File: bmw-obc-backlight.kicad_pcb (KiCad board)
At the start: 2 copper layers, 12 x 59 mm, 4 parts, among them J1 Conn_01x02

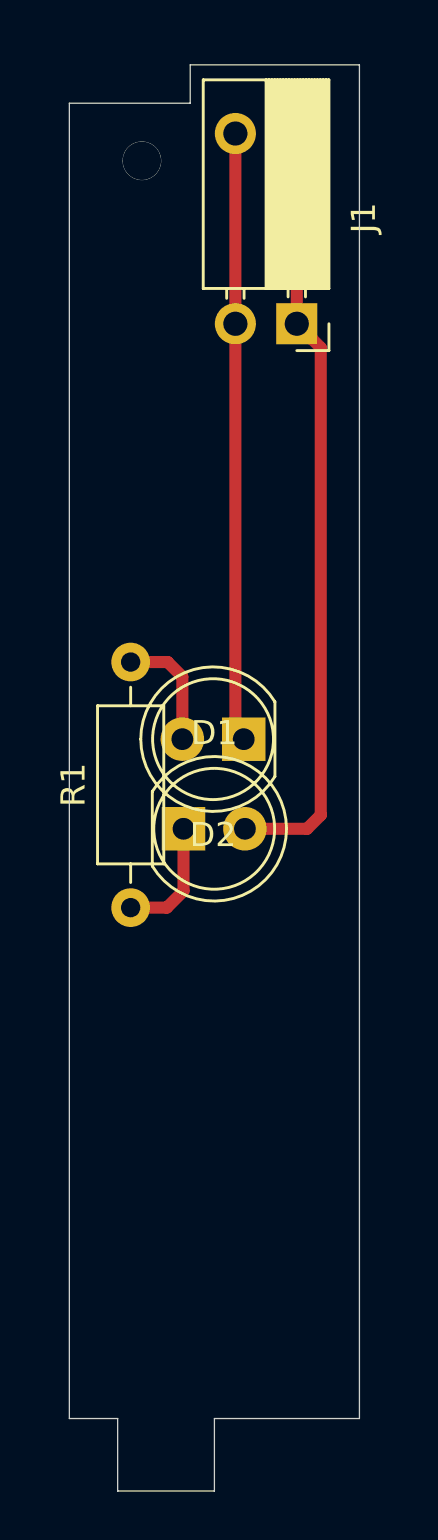
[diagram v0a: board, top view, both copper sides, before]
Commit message: Swapped resistor to SMT. There isn't enough space for a through hole unless it's between the LED legs.
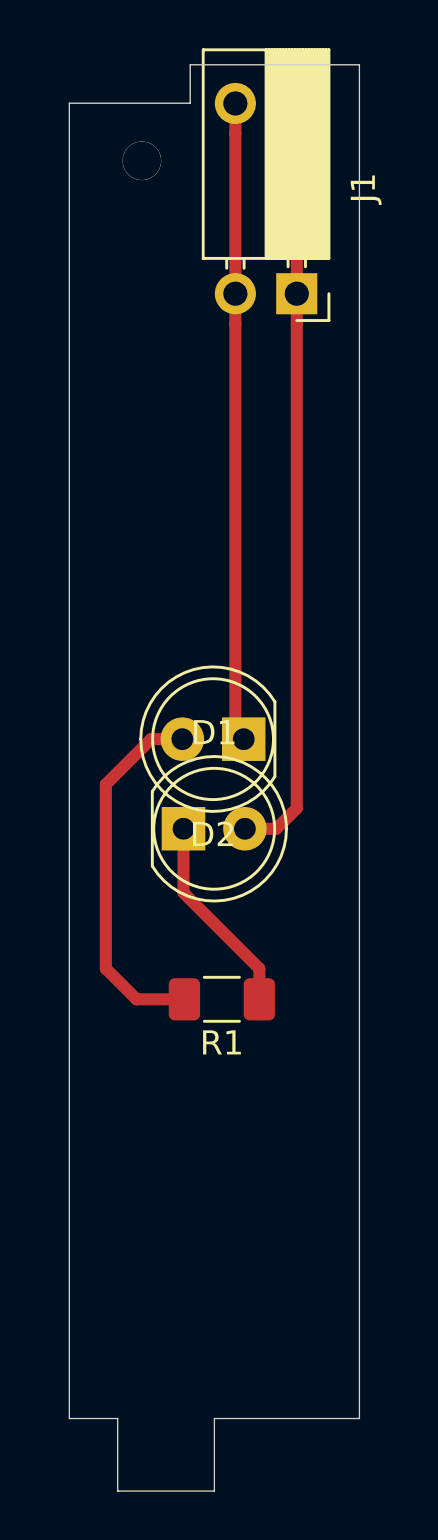
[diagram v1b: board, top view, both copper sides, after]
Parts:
- R1: footprint Resistor_THT:R_Axial_DIN0207_L6.3mm_D2.5mm_P10.16mm_Horizontal -> Resistor_SMD:R_1206_3216Metric_Pad1.30x1.75mm_HandSolder
- moved R1 5.35 mm to (21.3, 52.1), turned to 180 degrees
- moved J1 1.24 mm to (24.4, 22.9)
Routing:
- net Net-(D2-Pad2): track 4.97 -> 15.3 mm
- net Net-(D1-Pad1): track 5.04 -> 8.35 mm
- net Net-(D2-Pad1): track 25.2 -> 26.4 mm
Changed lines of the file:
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@@
     (thickness 1.6)
     (drawings 11)
-    (tracks 15)
+    (tracks 18)
     (zones 0)
     (modules 4)
@@
     (pad_to_mask_clearance 0)
     (aux_axis_origin 0 0)
-    (visible_elements FFFFFF7F)
+    (visible_elements 7FFFFFFF)
     (pcbplotparams
       (layerselection 0x010f0_ffffffff)
@@
     (add_net "Net-(D2-Pad2)")
   )
+  (module Resistor_SMD:R_1206_3216Metric_Pad1.30x1.75mm_HandSolder (layer F.Cu)
+    (at 21.31 52.07 180)
+    (descr "Resistor SMD 1206 (3216 Metric), square (rectangular) end terminal, IPC_7351 nominal with elongated pad for handsoldering. (Body size source: IPC-SM-782 page 72, https://www.pcb-3d.com/wordpress/wp-content/uploads/ipc-sm-782a_amendment_1_and_2.pdf), generated with kicad-footprint-generator")
+    (tags "resistor handsolder")
+    (attr smd)
+    (fp_text reference R1 (at 0 -1.82) (layer F.SilkS)
+      (effects (font (size 1 1) (thickness 0.15)))
+    )
+    (fp_text value 10000 (at 0 1.82) (layer F.Fab)
+      (effects (font (size 1 1) (thickness 0.15)))
+    )
+    (fp_text user %R (at 0 0) (layer F.Fab)
+      (effects (font (size 0.8 0.8) (thickness 0.12)))
+    )
+    (fp_line (start -1.6 0.8) (end -1.6 -0.8) (layer F.Fab) (width 0.1))
+    (fp_line (start -1.6 -0.8) (end 1.6 -0.8) (layer F.Fab) (width 0.1))
+    (fp_line (start 1.6 -0.8) (end 1.6 0.8) (layer F.Fab) (width 0.1))
+    (fp_line (start 1.6 0.8) (end -1.6 0.8) (layer F.Fab) (width 0.1))
+    (fp_line (start -0.727064 -0.91) (end 0.727064 -0.91) (layer F.SilkS) (width 0.12))
+    (fp_line (start -0.727064 0.91) (end 0.727064 0.91) (layer F.SilkS) (width 0.12))
+    (fp_line (start -2.45 1.12) (end -2.45 -1.12) (layer F.CrtYd) (width 0.05))
+    (fp_line (start -2.45 -1.12) (end 2.45 -1.12) (layer F.CrtYd) (width 0.05))
+    (fp_line (start 2.45 -1.12) (end 2.45 1.12) (layer F.CrtYd) (width 0.05))
+    (fp_line (start 2.45 1.12) (end -2.45 1.12) (layer F.CrtYd) (width 0.05))
+    (pad 2 smd roundrect (at 1.55 0 180) (size 1.3 1.75) (layers F.Cu F.Paste F.Mask) (roundrect_rratio 0.1923076923076923)
+      (net 3 "Net-(D2-Pad2)"))
+    (pad 1 smd roundrect (at -1.55 0 180) (size 1.3 1.75) (layers F.Cu F.Paste F.Mask) (roundrect_rratio 0.1923076923076923)
+      (net 1 "Net-(D1-Pad1)"))
+    (model ${KISYS3DMOD}/Resistor_SMD.3dshapes/R_1206_3216Metric.wrl
+      (at (xyz 0 0 0))
+      (scale (xyz 1 1 1))
+      (rotate (xyz 0 0 0))
+    )
+  )
   (module LED_THT:LED_D5.0mm (layer F.Cu)
     (at 19.722532 45.015429)
@@
       (effects (font (size 1 1) (thickness 0.15)))
     )
-    (fp_text user %R (at 1.25 0) (layer F.Fab)
-      (effects (font (size 0.8 0.8) (thickness 0.2)))
-    )
-    (fp_arc (start 1.27 0) (end -1.29 1.54483) (angle -148.9) (layer F.SilkS) (width 0.12))
-    (fp_arc (start 1.27 0) (end -1.29 -1.54483) (angle 148.9) (layer F.SilkS) (width 0.12))
-    (fp_arc (start 1.27 0) (end -1.23 -1.469694) (angle 299.1) (layer F.Fab) (width 0.1))
     (fp_circle (center 1.27 0) (end 3.77 0) (layer F.Fab) (width 0.1))
     (fp_circle (center 1.27 0) (end 3.77 0) (layer F.SilkS) (width 0.12))
@@
     (fp_line (start 4.5 3.25) (end 4.5 -3.25) (layer F.CrtYd) (width 0.05))
     (fp_line (start 4.5 -3.25) (end -1.95 -3.25) (layer F.CrtYd) (width 0.05))
+    (fp_text user %R (at 1.25 0) (layer F.Fab)
+      (effects (font (size 0.8 0.8) (thickness 0.2)))
+    )
+    (fp_arc (start 1.27 0) (end -1.29 1.54483) (angle -148.9) (layer F.SilkS) (width 0.12))
+    (fp_arc (start 1.27 0) (end -1.29 -1.54483) (angle 148.9) (layer F.SilkS) (width 0.12))
+    (fp_arc (start 1.27 0) (end -1.23 -1.469694) (angle 299.1) (layer F.Fab) (width 0.1))
     (pad 2 thru_hole circle (at 2.54 0 180) (size 1.8 1.8) (drill 0.9) (layers *.Cu *.Mask)
       (net 3 "Net-(D2-Pad2)"))
@@
   )
   (module bmw-obc-backlight-footprints:TE_2Position_2.54mmPitch_Horizontal_Header (layer F.Cu)
-    (at 24.408508 24.123633 270)
+    (at 24.408508 22.88 270)
     (descr "Through hole angled socket strip, 1x02, 2.54mm pitch, 8.51mm socket length, single row (from Kicad 4.0.7), script generated")
     (tags "Through hole angled socket strip THT 1x02 2.54mm single row")
@@
     )
   )
-  (module Resistor_THT:R_Axial_DIN0207_L6.3mm_D2.5mm_P10.16mm_Horizontal (layer F.Cu)
-    (at 17.536044 48.277354 90)
-    (descr "Resistor, Axial_DIN0207 series, Axial, Horizontal, pin pitch=10.16mm, 0.25W = 1/4W, length*diameter=6.3*2.5mm^2, http://cdn-reichelt.de/documents/datenblatt/B400/1_4W%23YAG.pdf")
-    (tags "Resistor Axial_DIN0207 series Axial Horizontal pin pitch 10.16mm 0.25W = 1/4W length 6.3mm diameter 2.5mm")
-    (fp_text reference R1 (at 5.08 -2.37 90) (layer F.SilkS)
-      (effects (font (size 1 1) (thickness 0.15)))
-    )
-    (fp_text value 10000 (at 5.08 2.37 90) (layer F.Fab)
-      (effects (font (size 1 1) (thickness 0.15)))
-    )
-    (fp_line (start 11.21 -1.5) (end -1.05 -1.5) (layer F.CrtYd) (width 0.05))
-    (fp_line (start 11.21 1.5) (end 11.21 -1.5) (layer F.CrtYd) (width 0.05))
-    (fp_line (start -1.05 1.5) (end 11.21 1.5) (layer F.CrtYd) (width 0.05))
-    (fp_line (start -1.05 -1.5) (end -1.05 1.5) (layer F.CrtYd) (width 0.05))
-    (fp_line (start 9.12 0) (end 8.35 0) (layer F.SilkS) (width 0.12))
-    (fp_line (start 1.04 0) (end 1.81 0) (layer F.SilkS) (width 0.12))
-    (fp_line (start 8.35 -1.37) (end 1.81 -1.37) (layer F.SilkS) (width 0.12))
-    (fp_line (start 8.35 1.37) (end 8.35 -1.37) (layer F.SilkS) (width 0.12))
-    (fp_line (start 1.81 1.37) (end 8.35 1.37) (layer F.SilkS) (width 0.12))
-    (fp_line (start 1.81 -1.37) (end 1.81 1.37) (layer F.SilkS) (width 0.12))
-    (fp_line (start 10.16 0) (end 8.23 0) (layer F.Fab) (width 0.1))
-    (fp_line (start 0 0) (end 1.93 0) (layer F.Fab) (width 0.1))
-    (fp_line (start 8.23 -1.25) (end 1.93 -1.25) (layer F.Fab) (width 0.1))
-    (fp_line (start 8.23 1.25) (end 8.23 -1.25) (layer F.Fab) (width 0.1))
-    (fp_line (start 1.93 1.25) (end 8.23 1.25) (layer F.Fab) (width 0.1))
-    (fp_line (start 1.93 -1.25) (end 1.93 1.25) (layer F.Fab) (width 0.1))
-    (fp_text user %R (at 5.08 0 90) (layer F.Fab)
-      (effects (font (size 1 1) (thickness 0.15)))
-    )
-    (pad 1 thru_hole circle (at 0 0 90) (size 1.6 1.6) (drill 0.8) (layers *.Cu *.Mask)
-      (net 1 "Net-(D1-Pad1)"))
-    (pad 2 thru_hole oval (at 10.16 0 90) (size 1.6 1.6) (drill 0.8) (layers *.Cu *.Mask)
-      (net 3 "Net-(D2-Pad2)"))
-    (model ${KISYS3DMOD}/Resistor_THT.3dshapes/R_Axial_DIN0207_L6.3mm_D2.5mm_P10.16mm_Horizontal.wrl
-      (at (xyz 0 0 0))
-      (scale (xyz 1 1 1))
-      (rotate (xyz 0 0 0))
-    )
-  )
   (gr_text "OBC LED\nRev 0 (2021)\nBrady Dow " (at 20.32 59.69 90) (layer B.SilkS)
     (effects (font (size 1.5 1.5) (thickness 0.3)) (justify mirror))
@@
   (gr_line (start 15 15) (end 15 69.4125) (layer Edge.Cuts) (width 0.05))
   (via (at 18 17.38125) (size 1.6) (drill 1.5875) (layers F.Cu B.Cu) (net 0))
-  (segment (start 17.536044 48.277354) (end 19.032646 48.277354) (width 0.5) (layer F.Cu) (net 1))
-  (segment (start 19.722532 47.587468) (end 19.722532 45.015429) (width 0.5) (layer F.Cu) (net 1))
-  (segment (start 19.032646 48.277354) (end 19.722532 47.587468) (width 0.5) (layer F.Cu) (net 1))
-  (segment (start 22.262532 45.015429) (end 24.834571 45.015429) (width 0.5) (layer F.Cu) (net 2))
-  (segment (start 24.834571 45.015429) (end 25.4 44.45) (width 0.5) (layer F.Cu) (net 2))
-  (segment (start 25.4 25.115125) (end 24.408508 24.123633) (width 0.5) (layer F.Cu) (net 2))
-  (segment (start 25.4 44.45) (end 25.4 25.115125) (width 0.5) (layer F.Cu) (net 2))
+  (segment (start 22.86 52.07) (end 22.86 50.8) (width 0.5) (layer F.Cu) (net 1))
+  (segment (start 19.722532 47.662532) (end 19.722532 45.015429) (width 0.5) (layer F.Cu) (net 1))
+  (segment (start 22.86 50.8) (end 19.722532 47.662532) (width 0.5) (layer F.Cu) (net 1))
   (segment (start 24.408508 24.123633) (end 24.408508 16.253633) (width 0.5) (layer F.Cu) (net 2))
-  (segment (start 19.674151 41.308193) (end 19.674151 38.724151) (width 0.5) (layer F.Cu) (net 3))
-  (segment (start 19.067354 38.117354) (end 17.536044 38.117354) (width 0.5) (layer F.Cu) (net 3))
-  (segment (start 19.674151 38.724151) (end 19.067354 38.117354) (width 0.5) (layer F.Cu) (net 3))
+  (segment (start 24.408508 24.123633) (end 24.408508 44.171492) (width 0.5) (layer F.Cu) (net 2))
+  (segment (start 23.564571 45.015429) (end 22.262532 45.015429) (width 0.5) (layer F.Cu) (net 2))
+  (segment (start 24.408508 44.171492) (end 23.564571 45.015429) (width 0.5) (layer F.Cu) (net 2))
+  (segment (start 24.408508 16.253633) (end 24.408508 15.01) (width 0.5) (layer F.Cu) (net 2))
+  (segment (start 19.76 52.07) (end 17.78 52.07) (width 0.5) (layer F.Cu) (net 3))
+  (segment (start 17.78 52.07) (end 16.51 50.8) (width 0.5) (layer F.Cu) (net 3))
+  (segment (start 16.51 50.8) (end 16.51 43.18) (width 0.5) (layer F.Cu) (net 3))
+  (segment (start 18.381807 41.308193) (end 19.674151 41.308193) (width 0.5) (layer F.Cu) (net 3))
+  (segment (start 16.51 43.18) (end 18.381807 41.308193) (width 0.5) (layer F.Cu) (net 3))
   (segment (start 21.868508 40.96255) (end 22.214151 41.308193) (width 0.25) (layer F.Cu) (net 4))
   (segment (start 21.868508 24.123633) (end 21.868508 40.96255) (width 0.5) (layer F.Cu) (net 4))
   (segment (start 21.868508 24.123633) (end 21.868508 16.253633) (width 0.5) (layer F.Cu) (net 4))
+  (segment (start 21.868508 16.253633) (end 21.868508 15.01) (width 0.5) (layer F.Cu) (net 4))
 )

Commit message: Swap to surface mount LEDs and add JLC manufacturing information
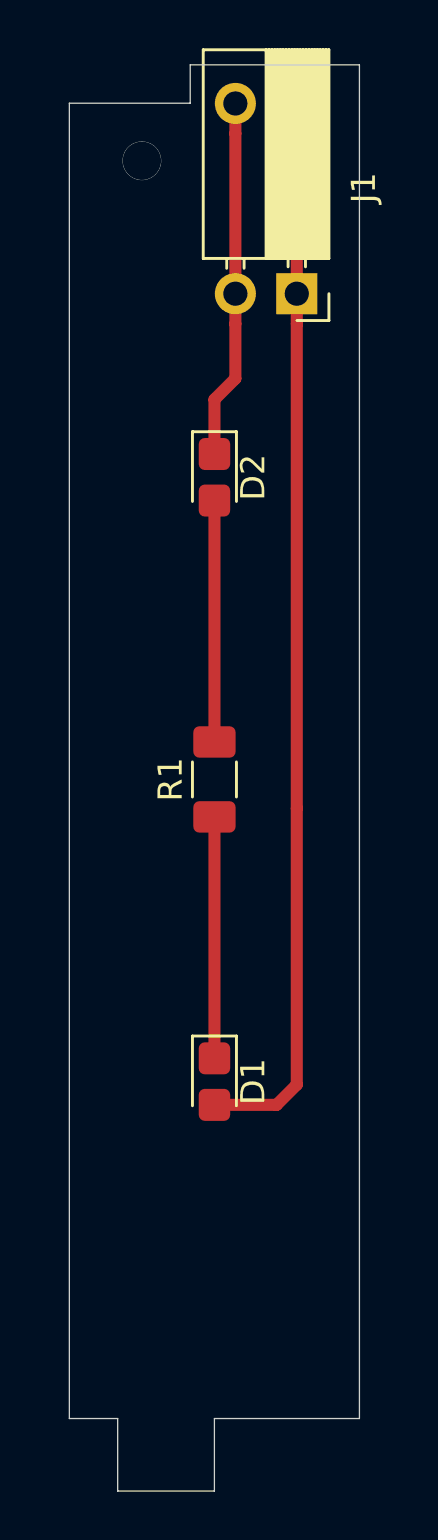
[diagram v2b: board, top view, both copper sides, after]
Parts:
- D1, D2: footprint LED_THT:LED_D5.0mm -> LED_SMD:LED_0805_2012Metric_Castellated
- moved D2 10.9 mm to (21.0, 30.5), turned to 270 degrees
- moved D1 10.5 mm to (21.0, 55.5), turned to 270 degrees
- moved R1 9.10 mm to (21.0, 43.0), turned to 90 degrees
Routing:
- net Net-(D1-Pad2): track 31.7 -> 44.3 mm
- net Net-(D2-Pad1): track 26.4 -> 14.9 mm
- net Net-(D2-Pad2): track 15.3 -> 9.99 mm
- net Net-(D1-Pad1): track 8.35 -> 9.99 mm

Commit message: Changes for ordering
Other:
- board text added: "OBC LED Rev 1 (2022) Brady Dow"
- board text removed: "OBC LED Rev 0 (2021) Brady Dow"
